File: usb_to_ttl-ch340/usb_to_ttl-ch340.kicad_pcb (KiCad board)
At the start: 2 copper layers, 18 parts, among them J1 USB_OTG, J2 6_pin_header, U1 CH340G, Y1 12MHz

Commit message: düzeltme 2
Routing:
- net GNDREF: vias 0 -> 4

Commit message: düzeltme3
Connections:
- C1 pad 1: Net-(C1-Pad1) -> +5V
- D3 pad 2: Net-(C1-Pad1) -> +5V
- J2 pad 6: Net-(C1-Pad1) -> +5V
- R1 pad 1: Net-(C1-Pad1) -> +5V
- R2 pad 1: Net-(C1-Pad1) -> +5V
- U1 pad 16: Net-(C1-Pad1) -> +5V
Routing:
- net +5V: track 54.8 -> 115.0 mm, vias 2 -> 3
- net Net-(C1-Pad1): track 56.1 -> 0.00 mm

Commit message: son güncelleme
pcb tasarımında bazı ufak değişiklikler yapıldı .
sayfa ayarları yapıldı
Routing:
- net GNDREF: vias 4 -> 7
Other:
- board text added: "3V3"
- board text added: "5V"
- board text added: "Ethem KANDEMİR"
- board text added: "GND"
- board text added: "RND Electronic"
- board text added: "RST"
- board text added: "RXD"
- board text added: "TXD"
- board text added: "USB to TTL Converter"
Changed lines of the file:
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@@
   (general
     (thickness 1.6)
-    (drawings 4)
-    (tracks 168)
+    (drawings 13)
+    (tracks 172)
     (zones 0)
     (modules 18)
@@
   )
   (page A4)
+  (title_block
+    (title "usb to ttl dönüştürücü")
+    (date 2021-09-08)
+    (company "RND Electronic")
+  )
   (layers
     (0 F.Cu signal)
-    (31 B.Cu signal hide)
+    (31 B.Cu signal)
     (32 B.Adhes user)
     (33 F.Adhes user)
@@
     (last_trace_width 0.25)
     (trace_clearance 0.2)
-    (zone_clearance 0.254)
+    (zone_clearance 0.508)
     (zone_45_only no)
     (trace_min 0.2)
@@
     )
   )
+  (gr_text "Ethem\nKANDEMİR" (at 146.05 86.36) (layer B.SilkS)
+    (effects (font (size 1 1) (thickness 0.15)))
+  )
+  (gr_text "USB to TTL\nConverter" (at 120.65 78.74) (layer B.SilkS)
+    (effects (font (size 3 3) (thickness 0.7)))
+  )
+  (gr_text "RND\nElectronic" (at 147.32 87.63) (layer F.SilkS)
+    (effects (font (size 1 1) (thickness 0.15)))
+  )
+  (gr_text "5V\n" (at 145.365 81.28) (layer F.SilkS)
+    (effects (font (size 0.5 0.5) (thickness 0.1)))
+  )
+  (gr_text RST (at 145.365 80.3) (layer F.SilkS)
+    (effects (font (size 0.5 0.5) (thickness 0.1)))
+  )
+  (gr_text 3V3 (at 145.365 79.3) (layer F.SilkS)
+    (effects (font (size 0.5 0.5) (thickness 0.1)))
+  )
+  (gr_text TXD (at 145.365 78.3) (layer F.SilkS)
+    (effects (font (size 0.5 0.5) (thickness 0.1)))
+  )
+  (gr_text RXD (at 145.365 77.3) (layer F.SilkS)
+    (effects (font (size 0.5 0.5) (thickness 0.1)))
+  )
+  (gr_text GND (at 145.365 76.3) (layer F.SilkS)
+    (effects (font (size 0.5 0.5) (thickness 0.1)))
+  )
   (gr_line (start 93.98 90.17) (end 93.98 69.85) (layer Dwgs.User) (width 0.15))
   (gr_line (start 152.4 90.17) (end 93.98 90.17) (layer Dwgs.User) (width 0.15))
   (gr_line (start 152.4 69.85) (end 152.4 90.17) (layer Dwgs.User) (width 0.15))
   (gr_line (start 93.98 69.85) (end 152.4 69.85) (layer Dwgs.User) (width 0.15))
+  (via (at 105.41 80.7) (size 0.8) (drill 0.4) (layers F.Cu B.Cu) (net 1))
+  (via (at 129 72.8) (size 0.8) (drill 0.4) (layers F.Cu B.Cu) (net 1))
+  (segment (start 98.8225 82.51) (end 97.8225 83.51) (width 0.25) (layer B.Cu) (net 1))
+  (segment (start 100.5225 82.51) (end 98.8225 82.51) (width 0.25) (layer B.Cu) (net 1))
+  (segment (start 98.8225 77.51) (end 97.8225 76.51) (width 0.25) (layer B.Cu) (net 1))
+  (segment (start 100.5225 77.51) (end 98.8225 77.51) (width 0.25) (layer B.Cu) (net 1))
+  (segment (start 100.5225 82.51) (end 100.5225 81.31) (width 0.25) (layer F.Cu) (net 1))
+  (segment (start 97.8225 77.11) (end 97.8225 77.4375) (width 0.25) (layer F.Cu) (net 1))
+  (segment (start 97.8225 77.4375) (end 97.8225 79.01) (width 0.25) (layer F.Cu) (net 1))
+  (segment (start 97.8225 79.01) (end 97.8225 81.01) (width 0.25) (layer F.Cu) (net 1))
+  (segment (start 97.8225 81.01) (end 97.8225 82.91) (width 0.25) (layer F.Cu) (net 1))
+  (segment (start 97.8225 82.91) (end 97.8225 83.51) (width 0.25) (layer F.Cu) (net 1))
+  (segment (start 137.5675 76.2) (end 137.5675 80.01) (width 0.25) (layer F.Cu) (net 1))
+  (via (at 133.35 73.66) (size 0.8) (drill 0.4) (layers F.Cu B.Cu) (net 1))
+  (via (at 121.92 81.28) (size 0.8) (drill 0.4) (layers F.Cu B.Cu) (net 1))
+  (via (at 129.54 74.93) (size 0.8) (drill 0.4) (layers F.Cu B.Cu) (net 1))
+  (via (at 121.4 74.7) (size 0.8) (drill 0.4) (layers F.Cu B.Cu) (net 1))
+  (via (at 117.9 81.5) (size 0.8) (drill 0.4) (layers F.Cu B.Cu) (net 1))
+  (segment (start 138.8375 86.36) (end 140.97 86.36) (width 0.25) (layer F.Cu) (net 2))
+  (segment (start 140.97 86.36) (end 147.32 80.01) (width 0.25) (layer F.Cu) (net 2))
+  (via (at 135.89 86.36) (size 0.8) (drill 0.4) (layers F.Cu B.Cu) (net 3))
+  (via (at 111.76 76.2) (size 0.8) (drill 0.4) (layers F.Cu B.Cu) (net 3))
+  (segment (start 113.665 74.295) (end 113.665 73.725) (width 0.25) (layer F.Cu) (net 3))
+  (segment (start 111.76 76.2) (end 113.665 74.295) (width 0.25) (layer F.Cu) (net 3))
+  (segment (start 135.89 86.36) (end 138.0225 86.36) (width 0.25) (layer F.Cu) (net 3))
+  (segment (start 111.76 76.2) (end 125.73 76.2) (width 0.25) (layer B.Cu) (net 3))
+  (segment (start 135.89 86.36) (end 133.35 86.36) (width 0.25) (layer B.Cu) (net 3))
+  (segment (start 133.35 86.36) (end 125.73 78.74) (width 0.25) (layer B.Cu) (net 3))
+  (segment (start 125.73 78.74) (end 125.73 76.2) (width 0.25) (layer B.Cu) (net 3))
   (segment (start 109.855 72.75) (end 111.485 71.12) (width 0.25) (layer F.Cu) (net 4))
   (segment (start 109.855 73.725) (end 109.855 72.75) (width 0.25) (layer F.Cu) (net 4))
@@
   (segment (start 140.97 71.12) (end 140.97 71.878942) (width 0.25) (layer F.Cu) (net 4))
   (segment (start 131.2175 72.39) (end 131.2175 76.2) (width 0.25) (layer F.Cu) (net 4))
-  (via (at 129 72.8) (size 0.8) (drill 0.4) (layers F.Cu B.Cu) (net 1))
-  (segment (start 98.8225 82.51) (end 97.8225 83.51) (width 0.25) (layer B.Cu) (net 1))
-  (segment (start 100.5225 82.51) (end 98.8225 82.51) (width 0.25) (layer B.Cu) (net 1))
-  (segment (start 98.8225 77.51) (end 97.8225 76.51) (width 0.25) (layer B.Cu) (net 1))
-  (segment (start 100.5225 77.51) (end 98.8225 77.51) (width 0.25) (layer B.Cu) (net 1))
-  (segment (start 100.5225 82.51) (end 100.5225 81.31) (width 0.25) (layer F.Cu) (net 1))
-  (segment (start 97.8225 77.11) (end 97.8225 77.4375) (width 0.25) (layer F.Cu) (net 1))
-  (segment (start 97.8225 77.4375) (end 97.8225 79.01) (width 0.25) (layer F.Cu) (net 1))
-  (segment (start 97.8225 79.01) (end 97.8225 81.01) (width 0.25) (layer F.Cu) (net 1))
-  (segment (start 97.8225 81.01) (end 97.8225 82.91) (width 0.25) (layer F.Cu) (net 1))
-  (segment (start 97.8225 82.91) (end 97.8225 83.51) (width 0.25) (layer F.Cu) (net 1))
-  (segment (start 137.5675 76.2) (end 137.5675 80.01) (width 0.25) (layer F.Cu) (net 1))
-  (via (at 133.35 73.66) (size 0.8) (drill 0.4) (layers F.Cu B.Cu) (net 1))
-  (via (at 121.92 81.28) (size 0.8) (drill 0.4) (layers F.Cu B.Cu) (net 1))
-  (via (at 129.54 74.93) (size 0.8) (drill 0.4) (layers F.Cu B.Cu) (net 1))
   (via (at 110.4 76.2) (size 0.8) (drill 0.4) (layers F.Cu B.Cu) (net 4))
-  (segment (start 138.8375 86.36) (end 140.97 86.36) (width 0.25) (layer F.Cu) (net 2))
-  (segment (start 140.97 86.36) (end 147.32 80.01) (width 0.25) (layer F.Cu) (net 2))
-  (via (at 135.89 86.36) (size 0.8) (drill 0.4) (layers F.Cu B.Cu) (net 3))
-  (via (at 111.76 76.2) (size 0.8) (drill 0.4) (layers F.Cu B.Cu) (net 3))
-  (segment (start 113.665 74.295) (end 113.665 73.725) (width 0.25) (layer F.Cu) (net 3))
-  (segment (start 111.76 76.2) (end 113.665 74.295) (width 0.25) (layer F.Cu) (net 3))
-  (segment (start 135.89 86.36) (end 138.0225 86.36) (width 0.25) (layer F.Cu) (net 3))
-  (segment (start 111.76 76.2) (end 125.73 76.2) (width 0.25) (layer B.Cu) (net 3))
-  (segment (start 135.89 86.36) (end 133.35 86.36) (width 0.25) (layer B.Cu) (net 3))
-  (segment (start 133.35 86.36) (end 125.73 78.74) (width 0.25) (layer B.Cu) (net 3))
-  (segment (start 125.73 78.74) (end 125.73 76.2) (width 0.25) (layer B.Cu) (net 3))
   (via (at 102.87 80.01) (size 0.8) (drill 0.4) (layers F.Cu B.Cu) (net 4))
   (via (at 134.62 76.2) (size 0.8) (drill 0.4) (layers F.Cu B.Cu) (net 4))
@@
   (via (at 134.62 78.74) (size 0.8) (drill 0.4) (layers F.Cu B.Cu) (net 7))
   (segment (start 118.55 78.87) (end 118.745 78.675) (width 0.25) (layer F.Cu) (net 7))
-  (segment (start 118.55 85.09) (end 118.55 78.87) (width 0.25) (layer F.Cu) (net 7))
+  (segment (start 118.55 85.09) (end 118.55 80.84) (width 0.25) (layer F.Cu) (net 7))
   (segment (start 135.89 80.01) (end 134.62 78.74) (width 0.25) (layer F.Cu) (net 7))
   (segment (start 136.7525 80.01) (end 135.89 80.01) (width 0.25) (layer F.Cu) (net 7))
@@
   (segment (start 130.81 82.55) (end 126.18001 77.92001) (width 0.25) (layer B.Cu) (net 7))
   (segment (start 134.62 78.74) (end 130.81 82.55) (width 0.25) (layer B.Cu) (net 7))
+  (segment (start 118.55 80.84) (end 118.55 78.87) (width 0.25) (layer F.Cu) (net 7))
   (via (at 127 72.39) (size 0.8) (drill 0.4) (layers F.Cu B.Cu) (net 8))
   (via (at 129.54 78.74) (size 0.8) (drill 0.4) (layers F.Cu B.Cu) (net 8))

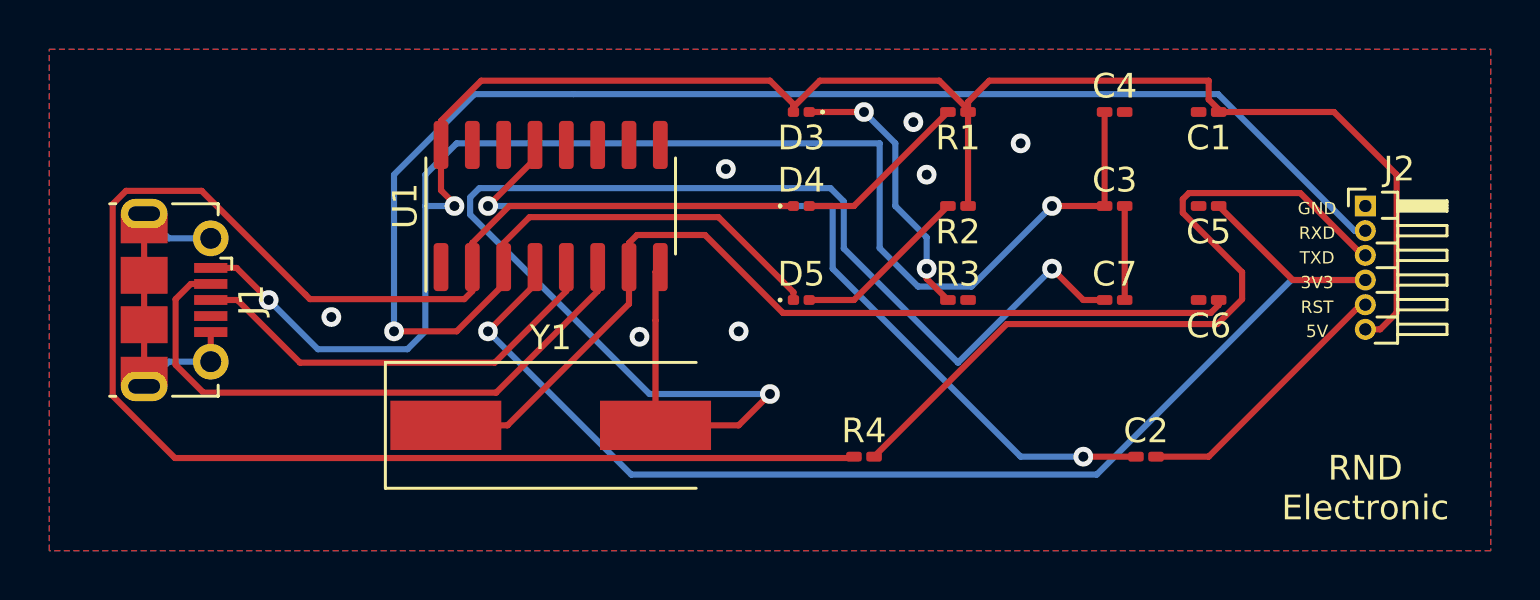
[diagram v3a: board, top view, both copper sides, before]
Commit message: düzeltme
belirtilen hatalar giderilmeye çalışıldı
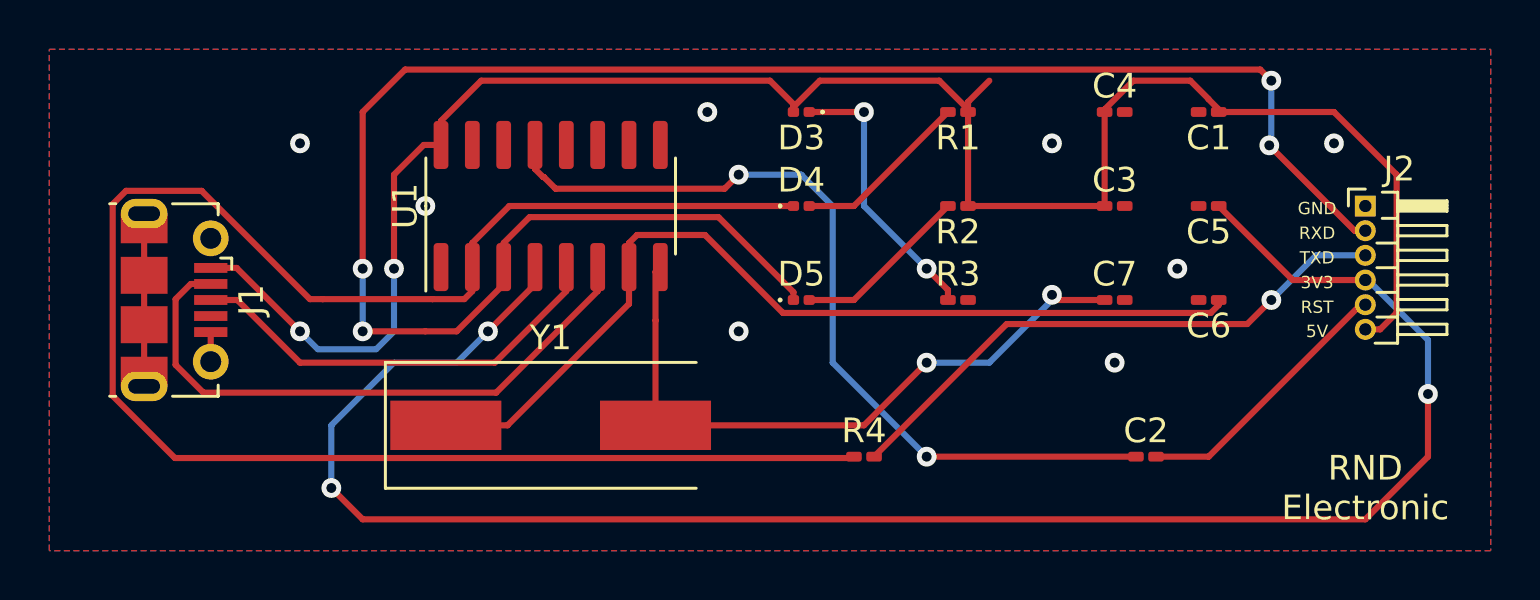
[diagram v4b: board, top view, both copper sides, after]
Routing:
- net +5V: track 115.0 -> 78.8 mm, vias 3 -> 2
- net Net-(C7-Pad1): track 59.6 -> 26.9 mm
- net +3V3: track 51.8 -> 75.4 mm, vias 1 -> 3
- net GNDREF: track 17.6 -> 7.60 mm, vias 7 -> 8
- net Net-(J2-Pad3): track 31.2 -> 23.4 mm, vias 0 -> 1
- net RXD: track 70.0 -> 76.5 mm, vias 1 -> 4

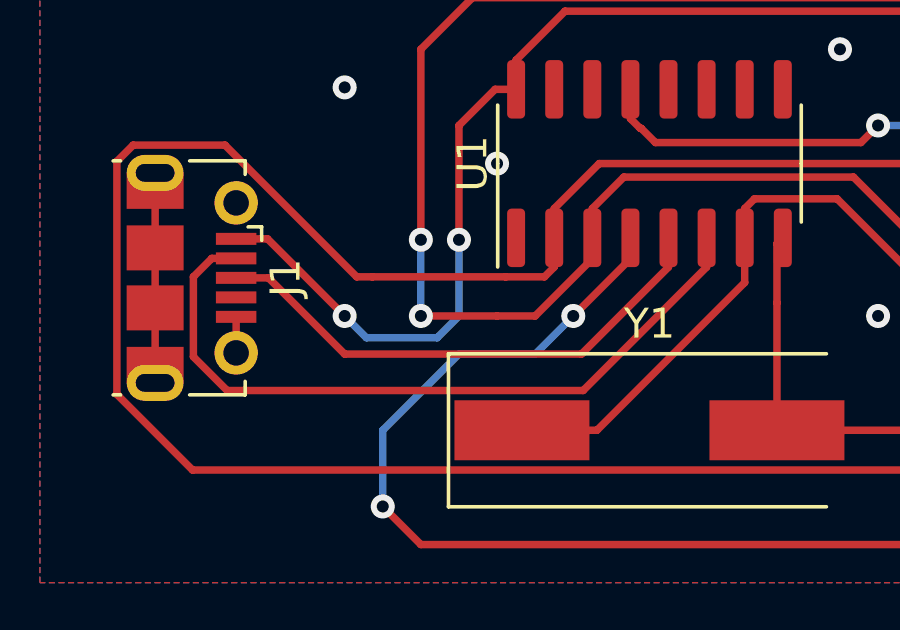
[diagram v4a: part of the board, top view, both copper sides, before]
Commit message: diffferential pair
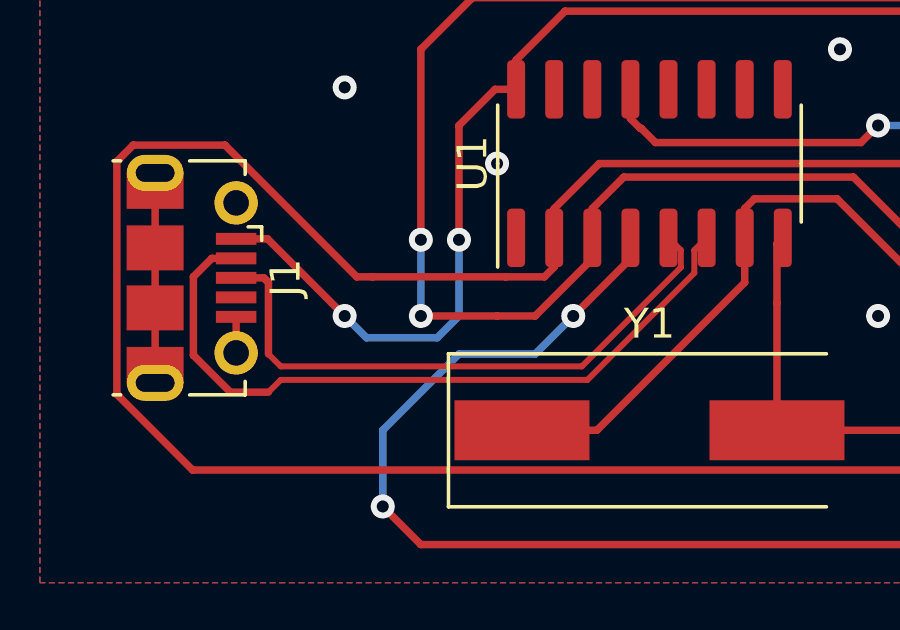
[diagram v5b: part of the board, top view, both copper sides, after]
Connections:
- net Net-(J1-Pad2) renamed /D-
- net Net-(J1-Pad3) renamed /D+
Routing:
- net /D+: track 17.6 -> 20.0 mm

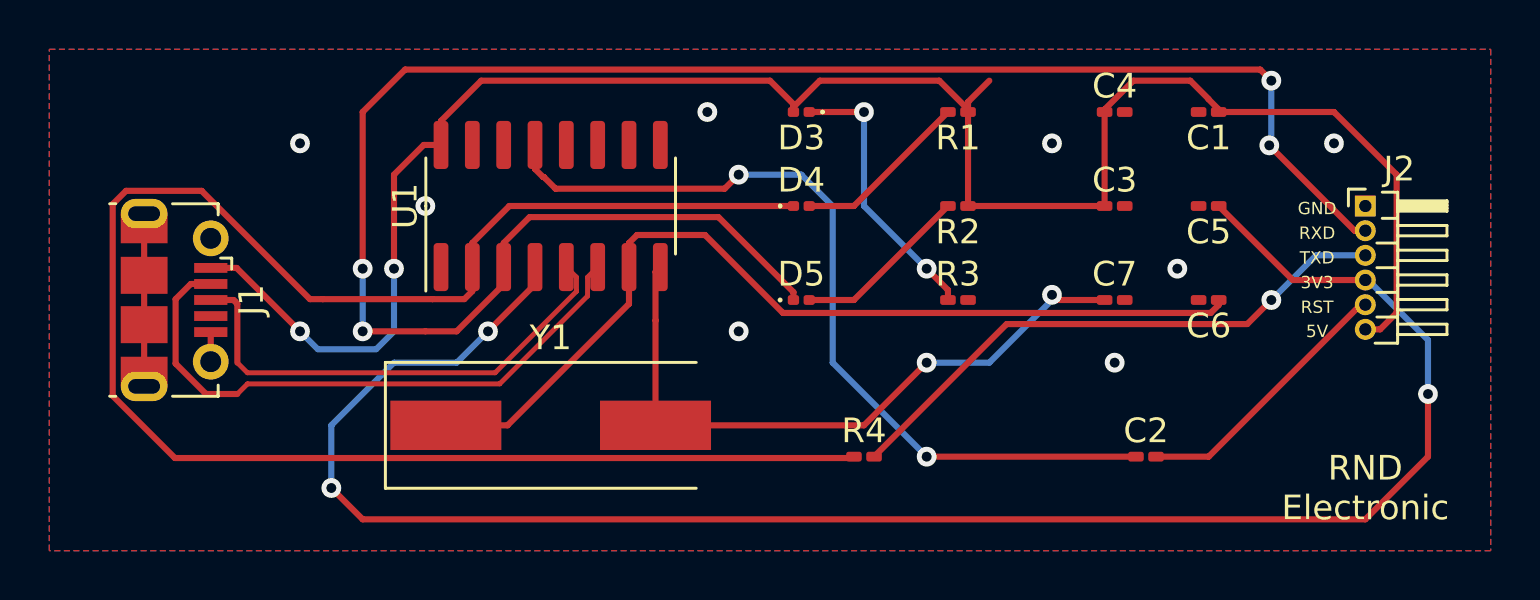
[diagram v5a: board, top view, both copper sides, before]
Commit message: yol kalınlığı
projelerde pcb yol kalınlıkları akım kapasitelerine göre yeniden düzenlendi
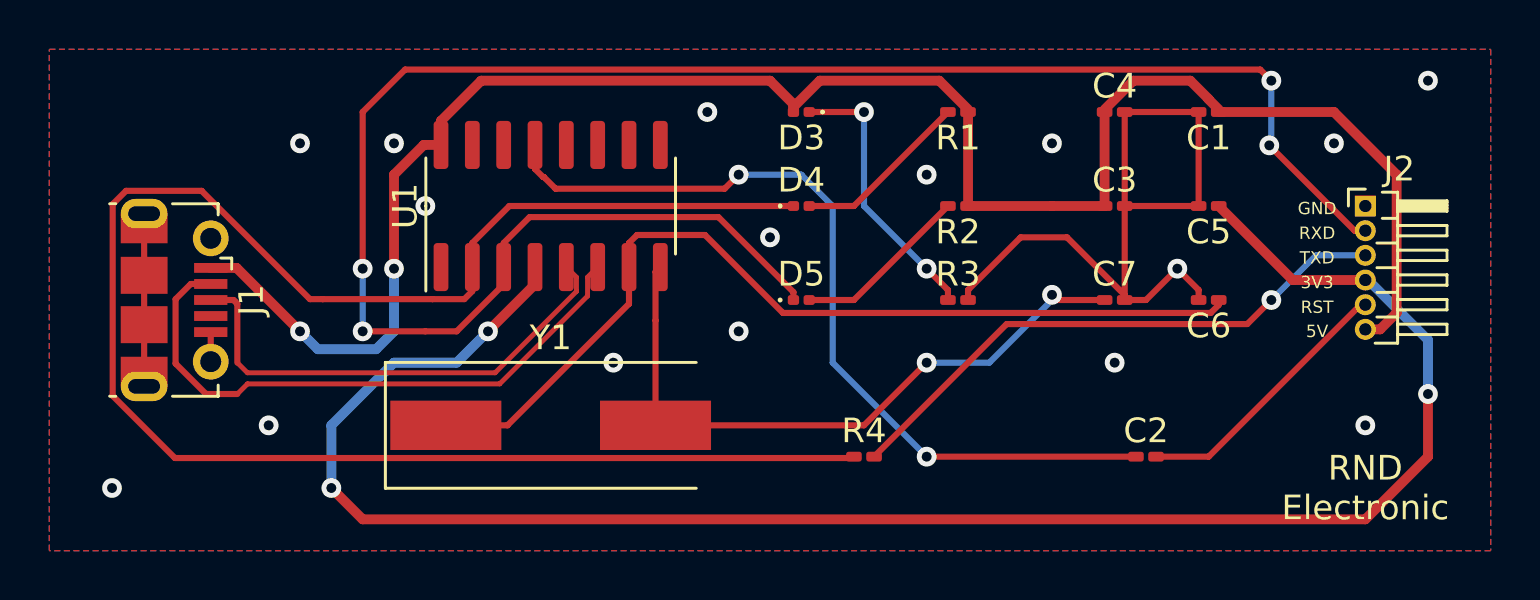
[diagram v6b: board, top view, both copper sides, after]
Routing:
- net GNDREF: track 7.60 -> 38.1 mm, vias 8 -> 16
- net +5V: track 78.8 -> 77.2 mm
